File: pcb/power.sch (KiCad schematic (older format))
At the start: 2 parts, among them U100 MCIMX7S5EVM08SC

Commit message: pcb: working on sch
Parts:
- added unit 10 of U100
- gave numbers to parts that had none: 1
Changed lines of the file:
@@
 $EndComp
 $Comp
-L symbols:LTC3456 U?
+L symbols:LTC3456 U1
 U 1 1 5DB1F8DC
 P 8050 3700
-F 0 "U?" H 8050 4765 50  0000 C CNN
+F 0 "U1" H 8050 4765 50  0000 C CNN
 F 1 "LTC3456" H 8050 4674 50  0000 C CNN
 F 2 "" H 8050 3700 50  0001 C CNN
@@
 	1    0    0    -1
 $EndComp
+$Comp
+L symbols:MCIMX7S5EVM08SC U100
+U 10 1 5D65C6CC
+P 5200 7800
+F 0 "U100" H 5200 10165 50  0000 C CNN
+F 1 "MCIMX7S5EVM08SC" H 5200 10074 50  0000 C CNN
+F 2 "footprints:BGA-541_25x25_19.0x19.0mm" H 5200 8500 50  0001 C CNN
+F 3 "" H 5200 8500 50  0001 C CNN
+	10   5200 7800
+	1    0    0    -1
+$EndComp

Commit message: pcb: working on sch
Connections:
- net GND: now reaches U100.AA10 (PCIE_VP)
- net GND: now also U100.AA11 (PCIE_VP_TX), U100.AA12 (PCIE_VP_RX), U100.H12 (USB_VDD_H_1P2), U100.Y10 (PCIE_VPH), U100.Y11 (PCIE_VPH_TX), U100.Y12 (PCIE_VPH_RX)
- no-connect marks 0 -> 4
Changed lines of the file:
@@
 	1    0    0    -1
 $EndComp
+NoConn ~ 3400 2200
+NoConn ~ 3400 2300
+NoConn ~ 3400 3100
+$Comp
+L power:GND #PWR?
+U 1 1 5D1F2E2F
+P 3500 6200
+F 0 "#PWR?" H 3500 5950 50  0001 C CNN
+F 1 "GND" H 3505 6027 50  0000 C CNN
+F 2 "" H 3500 6200 50  0001 C CNN
+F 3 "" H 3500 6200 50  0001 C CNN
+	1    3500 6200
+	1    0    0    -1
+$EndComp
+Wire Wire Line
+	3400 3300 3500 3300
+Wire Wire Line
+	3500 3300 3500 3400
+Wire Wire Line
+	3400 3400 3500 3400
+Connection ~ 3500 3400
+Wire Wire Line
+	3500 3400 3500 3500
+Wire Wire Line
+	3400 3500 3500 3500
+Connection ~ 3500 3500
+Wire Wire Line
+	3500 3500 3500 4700
+NoConn ~ 3400 4500
+Wire Wire Line
+	3400 4700 3500 4700
+Connection ~ 3500 4700
+Wire Wire Line
+	3500 4700 3500 6200
+Wire Wire Line
+	3400 2500 3500 2500
+Wire Wire Line
+	3500 2500 3500 2600
+Connection ~ 3500 3300
+Wire Wire Line
+	3400 2600 3500 2600
+Connection ~ 3500 2600
+Wire Wire Line
+	3500 2600 3500 2700
+Wire Wire Line
+	3400 2700 3500 2700
+Connection ~ 3500 2700
+Wire Wire Line
+	3500 2700 3500 3300
 $EndSCHEMATC

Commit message: pcb: finishing sch for r0.1
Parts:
- removed unit 10 of U100
- added BT: Battery, Battery:BatteryHolder_Keystone_2468_2xAAA, symbol Device:Battery
- added BT_Backup: CR2032, Battery:BatteryHolder_Keystone_1060_1x2032, symbol Device:Battery_Cell
- added C1, C10, C11, C13, C8: 4.7uF, Capacitor_SMD:C_0603_1608Metric, symbol Device:C
- added C12, C4, C9: 220pF, Capacitor_SMD:C_0402_1005Metric, symbol Device:C
- added C14, C2, C3, C7: 10uF, Capacitor_SMD:C_0603_1608Metric, symbol Device:C
- added C15, C16, C17, C18, C20, C21, C22, C23, C25, C26, C27, C28, C29, C30, C32, C33, C34, C35, C36, C37, C38: 220nF, Capacitor_SMD:C_0402_1005Metric, symbol Device:C
- added C19, C24, C5: 22uF, Capacitor_SMD:C_0603_1608Metric, symbol Device:C
- added C31, C39, C40, C41: 2.2uF, Capacitor_SMD:C_0402_1005Metric, symbol Device:C
- added C6: 1uF, Capacitor_SMD:C_0402_1005Metric, symbol Device:C
- added D1, D2: 1N5819, Diode_SMD:D_SOD-123, symbol Device:D_Shockley
- added L1, L3: 10uH, Inductor_SMD:L_Vishay_IHLP-4040, symbol Device:L
- added L2: 4.7uH, Inductor_SMD:L_Vishay_IHLP-4040, symbol Device:L
- added L4, L5: 3.3uH, Inductor_SMD:L_Vishay_IHLP-4040, symbol Device:L
- added L6: 120R, Inductor_SMD:L_0603_1608Metric, symbol Device:L
- added R1: 1K, Resistor_SMD:R_0603_1608Metric, symbol Device:R
- added R10: 130K, Resistor_SMD:R_0603_1608Metric, symbol Device:R
- added R11: 200K, Resistor_SMD:R_0603_1608Metric, symbol Device:R
- added R12, R4, R7: 0R05, Resistor_SMD:R_1210_3225Metric, symbol Device:R
- added R2, R5: 100K, Resistor_SMD:R_0603_1608Metric, symbol Device:R
- added R3, R6: 80.6K, Resistor_SMD:R_0603_1608Metric, symbol Device:R
- added R8: 147K, Resistor_SMD:R_0603_1608Metric, symbol Device:R
- added R9: 154K, Resistor_SMD:R_0603_1608Metric, symbol Device:R
- added U2, U3: LTC3549, Package_DFN_QFN:DFN-6-1EP_3x2mm_P0.5mm_EP1.65x1.35mm, symbol symbols:LTC3549
- U1: footprint (none) -> Package_DFN_QFN:VQFN-24-1EP_4x4mm_P0.5mm_EP2.45x2.45mm_ThermalVias
- U100: footprint (none) -> footprints:BGA-541_25x25_19.0x19.0mm
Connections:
- net GND: now also U1.3 (AGND), U1.6 (PGND), U100.A1 (GND), U100.A13 (GND), U100.A17 (GND), U100.A21 (GND), U100.A25 (GND), U100.A3 (GND), U100.A6 (GND), U100.A9 (GND), U100.AA1 (GND), U100.AA15 (GND), U100.AA2 (GND), U100.AA23 (GND), U100.AA6 (GND), U100.AA8 (GND), U100.AB12 (GND), U100.AB4 (GND), U100.AB5 (GND), U100.AB7 (GND), U100.AB9 (GND), U100.AC12 (GND), U100.AC15 (GND), U100.AC17 (GND), U100.AC19 (GND), U100.AC21 (GND), U100.AC23 (GND), U100.AC6 (GND), U100.AC9 (GND), U100.AD12 (GND), U100.AD2 (GND), U100.AD5 (GND), U100.AD7 (GND), U100.AD9 (GND), U100.AE1 (GND), U100.AE12 (GND), U100.AE24 (GND), U100.AE25 (GND), U100.AE5 (GND), U100.AE7 (GND), U100.AE9 (GND), U100.B13 (GND), U100.B17 (GND), U100.B21 (GND), U100.B3 (GND), U100.B6 (GND), U100.B9 (GND), U100.C13 (GND), U100.C15 (GND), U100.C16 (GND), U100.C18 (GND), U100.C19 (GND), U100.C9 (GND), U100.D1 (GND), U100.D10 (GND), U100.D2 (GND), U100.D22 (GND), U100.D4 (GND), U100.D7 (GND), U100.F11 (GND), U100.F13 (GND), U100.F7 (GND), U100.F8 (GND), U100.G11 (GND), U100.G13 (GND), U100.G15 (GND), U100.G17 (GND), U100.G19 (GND), U100.G22 (GND), U100.G4 (GND), U100.G7 (GND), U100.G9 (GND), U100.H1 (GND), U100.H2 (GND), U100.J19 (GND), U100.J7 (GND), U100.K10 (GND), U100.K12 (GND), U100.K14 (GND), U100.K16 (GND), U100.K22 (GND), U100.K4 (GND), U100.L11 (GND), U100.L13 (GND), U100.L15 (GND), U100.L19 (GND), U100.L7 (GND), U100.M10 (GND), U100.M12 (GND), U100.M14 (GND), U100.M16 (GND), U100.M24 (GND), U100.M25 (GND), U100.N11 (GND), U100.N13 (GND), U100.N15 (GND), U100.N19 (GND), U100.N4 (GND), U100.N7 (GND), U100.P10 (GND), U100.P12 (GND), U100.P14 (GND), U100.P16 (GND), U100.R11 (GND), U100.R13 (GND), U100.R15 (GND), U100.R19 (GND), U100.R20 (GND), U100.R21 (GND), U100.R23 (GND), U100.R7 (GND), U100.T10 (GND), U100.T12 (GND), U100.T14 (GND), U100.T16 (GND), U100.T20 (GND), U100.T4 (GND), U100.U11 (GND), U100.U19 (GND), U100.U20 (GND), U100.U23 (GND), U100.U7 (GND), U100.V20 (GND), U100.W1 (GND), U100.W11 (GND), U100.W13 (GND), U100.W15 (GND), U100.W17 (GND), U100.W19 (GND), U100.W2 (GND), U100.W20 (GND), U100.W23 (GND), U100.W4 (GND), U100.W7 (GND), U100.W9 (GND), U100.Y13 (GND), U100.Y14 (GND), U100.Y15 (GND), U100.Y16 (GND), U100.Y17 (GND), U100.Y18 (GND), U100.Y19 (GND), U100.Y6 (GND), BT.2 (-), BT_Backup.2 (-), C1.2, C10.2, C11.2, C13.2, C14.2, C15.2, C16.2, C17.2, C18.2, C19.2, C2.2, C20.2, C21.2, C22.2, C23.2, C24.2, C25.2, C26.2, C27.2, C28.2, C29.2, C3.2, C30.2, C31.2, C32.2, C33.2, C34.2, C35.2, C36.1, C37.1, C38.1, C39.1, C40.1, C41.1, C5.2, C6.2, C7.2, C8.2, R11.2, R3.1, R6.2, R9.2, U2.2 (GND), U2.4 (MODE), U2.7 (EP), U3.2 (GND), U3.4 (MODE), U3.7 (EP)
- net at U100.AA9 (VDDD_1P0_CAP): now also C36.2
- net at U100.AC5 (VDD_LPSR_1P0_CAP): now also C40.2
- net at U100.AD8 (VDD_SNVS_IN): now also D1.1 (K), D2.1 (K)
- net at U100.AE8 (VDD_SNVS_1P8_CAP): now also C39.2
- net +1V0: now reaches U100.C14 (VDD_SOC_IN)
- net +1V0: now also U100.C17 (VDD_ARM_IN), U100.C20 (VDD_ARM_IN), U100.D14 (VDD_SOC_IN), U100.D17 (VDD_ARM_IN), U100.D20 (VDD_ARM_IN), U100.F18 (VDD_SOC_IN), U100.F19 (VDD_SOC_IN), U100.F22 (VDD_ARM_IN), U100.F23 (VDD_ARM_IN), U100.F3 (VDD_SOC_IN), U100.F4 (VDD_SOC_IN), U100.J22 (VDD_ARM_IN), U100.J23 (VDD_ARM_IN), U100.J3 (VDD_SOC_IN), U100.J4 (VDD_SOC_IN), U100.M3 (VDD_SOC_IN), U100.M4 (VDD_SOC_IN), U100.P18 (VDD_SOC_IN), U100.R17 (VDD_SOC_IN), U100.R3 (VDD_SOC_IN), U100.R4 (VDD_SOC_IN), U100.T18 (VDD_SOC_IN), U100.U13 (VDD_SOC_IN), U100.U15 (VDD_SOC_IN), U100.U17 (VDD_SOC_IN), U100.V12 (VDD_SOC_IN), U100.V14 (VDD_SOC_IN), U100.V16 (VDD_SOC_IN), U100.V18 (VDD_SOC_IN), C14.1, C15.1, C16.1, C17.1, C18.1, C19.1, C20.1, C21.1, C22.1, C23.1, C24.1, C25.1, C26.1, C27.1, C28.1, C29.1, R12.1
- net at U100.H18 (MIPI_VREG_0P4V): now also C38.2
- net +3V3: now reaches U100.P8 (NVCC_GPIO1)
- net +3V3: now also U100.T8 (NVCC_GPIO2), C34.1, C35.1, C7.1, D2.2 (A), R7.1
- net at U100.V10 (PVCC_GPIO_CAP): now also C41.2
- net at U100.V3 (VDDA_1P0_CAP): now also C37.2
- net at U100.V6 (VDDA_1P8): now also U100.W5 (VDDA_1P8), C30.1, C31.1, L6.2
- net +1V8: now reaches U100.V8 (FUSE_FSOURCE)
- net +1V8: now also U100.W6 (VDD_LPSR_IN), C11.1, C2.1, C32.1, C33.1, C8.1, L6.1, R4.2, U2.1 (Vin), U2.5 (RUN), U3.1 (Vin), U3.5 (RUN)
- net at U1.1 (AIN): now also R2.1, R3.2
- net VBUS: now reaches U1.10 (USB)
- net VBUS: now also R1.2
- net at U1.12 (USBHP): now also R1.1
- net at U1.13 (SW2_BK): now also L3.2
- net at U1.14 (SW2_BST): now also L2.2
- net at U1.15 (VINT): now also C5.1, L3.1
- net at U1.16 (VMAIN): now also C6.1, R7.2
- net USB_SUSPEND: now reaches U1.18 (SUSPEND)
- net PWRKEY: now reaches U1.19 (PWRKEY)
- net BAT_LOW: now reaches U1.2 (AO)
- net PB_STAT: now reaches U1.20 (PBSTAT)
- net PMIC_ON_REQ: now reaches U1.21 (PWRON)
- net +BATT: now reaches U1.22 (MODE)
- net +BATT: now also U1.4 (VBAT), BT.1 (+), C1.1, L2.1, R2.2
- net POR: now reaches U1.23 (~RESET)
- net at U1.24 (FB1): now also C4.2, R5.2, R6.1
- net at U1.5 (SW1): now also L1.2
- net EXT_PWR_GOOD: now reaches U1.8 (~EXT_PWR)
- new net: C3.1, C4.1, L1.1, R4.1, R5.1
- new net: L5.1, U3.3 (SW)
- new net: C12.2, R10.2, R11.1, U3.6 (Vfb)
- new net: C12.1, C13.1, L5.2, R10.1, R12.2
- new net: L4.1, U2.3 (SW)
- new net: C9.2, R8.2, R9.1, U2.6 (Vfb)
- new net: BT_Backup.1 (+), D1.2 (A)
- new net +1V2: C10.1, C9.1, L4.2, R8.1
- no-connect marks 4 -> 9
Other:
- note added: "CAP for VDD_ARM"
- note added: "CAP for VDD_SOC"
- note added: "Maximum 150mA\n(Voltage drop 7.5mV)"
- note added: "Maximum 200mA\n(Voltage drop 10mV)"
- note added: "Vfb=0.611V"
- moved on the sheet: U1, U100A

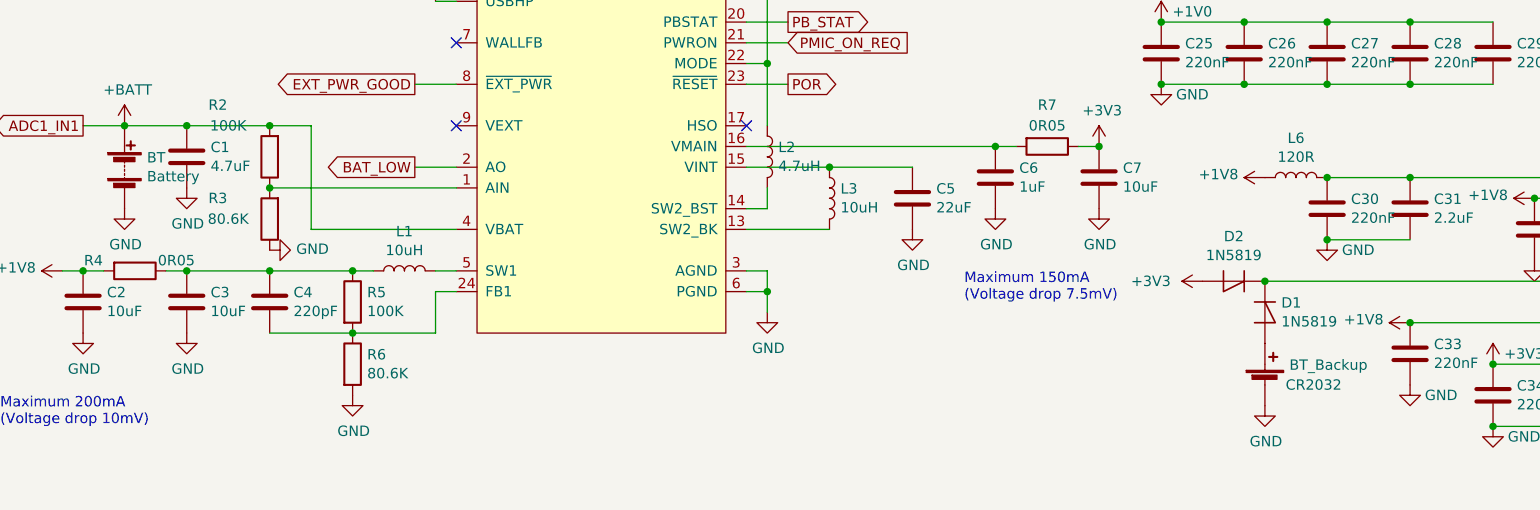
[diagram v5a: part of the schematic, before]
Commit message: pcb: initial netlist
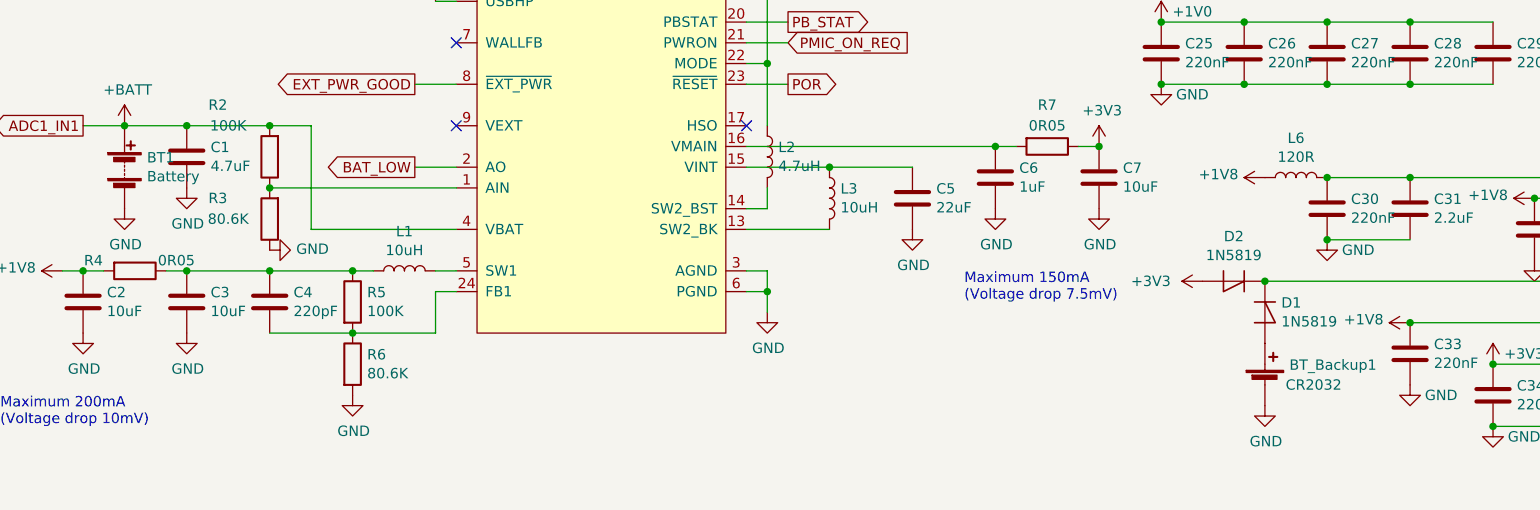
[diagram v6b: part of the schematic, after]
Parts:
- renumbered BT to BT1, BT_Backup to BT_Backup1
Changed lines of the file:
@@
 	3000 4850 3200 4850
 $Comp
-L Device:Battery BT
+L Device:Battery BT1
 U 1 1 5D2E55D4
 P 1600 4850
-F 0 "BT" H 1708 4896 50  0000 L CNN
+F 0 "BT1" H 1708 4896 50  0000 L CNN
 F 1 "Battery" H 1708 4805 50  0000 L CNN
 F 2 "Battery:BatteryHolder_Keystone_2468_2xAAA" V 1600 4910 50  0001 C CNN
@@
 	1400 4650 1600 4650
 $Comp
-L Device:Battery_Cell BT_Backup
+L Device:Battery_Cell BT_Backup1
 U 1 1 5D97B728
 P 7100 5900
-F 0 "BT_Backup" H 7218 5996 50  0000 L CNN
+F 0 "BT_Backup1" H 7218 5996 50  0000 L CNN
 F 1 "CR2032" H 7200 5900 50  0000 L CNN
 F 2 "Battery:BatteryHolder_Keystone_1060_1x2032" V 7100 5960 50  0001 C CNN
@@
 Connection ~ 7100 5400
 $Comp
-L power:GND #PWR?
+L power:GND #PWR0316
 U 1 1 5D98CDD3
 P 7100 6000
-F 0 "#PWR?" H 7100 5750 50  0001 C CNN
+F 0 "#PWR0316" H 7100 5750 50  0001 C CNN
 F 1 "GND" H 7105 5827 50  0000 C CNN
 F 2 "" H 7100 6000 50  0001 C CNN
@@
 $EndComp
 $Comp
-L power:+3V3 #PWR?
+L power:+3V3 #PWR0317
 U 1 1 5D98CE2E
 P 6800 5400
-F 0 "#PWR?" H 6800 5250 50  0001 C CNN
+F 0 "#PWR0317" H 6800 5250 50  0001 C CNN
 F 1 "+3V3" V 6800 5650 50  0000 C CNN
 F 2 "" H 6800 5400 50  0001 C CNN

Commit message: pcb: working on layout
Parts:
- added D3: LED, LED_THT:LED_D5.0mm, symbol Device:LED
- added R13: 1K, Resistor_SMD:R_0603_1608Metric, symbol Device:R
- added SW1: SW_SPDT, Button_Switch_SMD:SW_SPDT_PCM12, symbol Switch:SW_SPDT
- BT_Backup1: footprint Battery:BatteryHolder_Keystone_1060_1x2032 -> footprints:BatteryHolder_CR1220
- L1, L2, L3, L4, L5: footprint Inductor_SMD:L_Vishay_IHLP-4040 -> Inductor_SMD:L_Vishay_IHLP-1212
- L6: footprint Inductor_SMD:L_0603_1608Metric -> Inductor_SMD:L_0402_1005Metric
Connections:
- net EXT_PWR_GOOD: now also D3.2 (A)
- net GND: now also R13.2, SW1.3 (C)
- net PWRKEY renamed PWR_KEY
- net PWR_KEY: now also SW1.2 (B)
- new net: D3.1 (K), R13.1
- no-connect marks 9 -> 10
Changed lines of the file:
@@
 EXT_PWR_GOOD
 Wire Wire Line
-	3000 4450 3200 4450
+	3000 4450 3100 4450
 NoConn ~ 3200 4250
 NoConn ~ 3200 4650
@@
 F 0 "L1" V 3140 5350 50  0000 C CNN
 F 1 "10uH" V 3049 5350 50  0000 C CNN
-F 2 "Inductor_SMD:L_Vishay_IHLP-4040" H 2950 5350 50  0001 C CNN
+F 2 "Inductor_SMD:L_Vishay_IHLP-1212" H 2950 5350 50  0001 C CNN
 F 3 "~" H 2950 5350 50  0001 C CNN
 	1    2950 5350
@@
 	1500 5350 1400 5350
 NoConn ~ 4600 3750
-Text GLabel 4800 3950 2    50   Input ~ 0
-PWRKEY
 Text GLabel 4800 4150 2    50   Output ~ 0
 PB_STAT
@@
 Wire Wire Line
 	4600 4150 4800 4150
-Wire Wire Line
-	4600 3950 4800 3950
 NoConn ~ 4600 4650
 $Comp
@@
 F 0 "L3" H 5053 5046 50  0000 L CNN
 F 1 "10uH" H 5053 4955 50  0000 L CNN
-F 2 "Inductor_SMD:L_Vishay_IHLP-4040" H 5000 5000 50  0001 C CNN
+F 2 "Inductor_SMD:L_Vishay_IHLP-1212" H 5000 5000 50  0001 C CNN
 F 3 "~" H 5000 5000 50  0001 C CNN
 	1    5000 5000
@@
 F 0 "L2" H 4753 4846 50  0000 L CNN
 F 1 "4.7uH" H 4753 4755 50  0000 L CNN
-F 2 "Inductor_SMD:L_Vishay_IHLP-4040" H 4700 4800 50  0001 C CNN
+F 2 "Inductor_SMD:L_Vishay_IHLP-1212" H 4700 4800 50  0001 C CNN
 F 3 "~" H 4700 4800 50  0001 C CNN
 	1    4700 4800
@@
 F 0 "L5" V 7240 1700 50  0000 C CNN
 F 1 "3.3uH" V 7149 1700 50  0000 C CNN
-F 2 "Inductor_SMD:L_Vishay_IHLP-4040" H 7050 1700 50  0001 C CNN
+F 2 "Inductor_SMD:L_Vishay_IHLP-1212" H 7050 1700 50  0001 C CNN
 F 3 "~" H 7050 1700 50  0001 C CNN
 	1    7050 1700
@@
 F 0 "L4" V 3640 1700 50  0000 C CNN
 F 1 "3.3uH" V 3549 1700 50  0000 C CNN
-F 2 "Inductor_SMD:L_Vishay_IHLP-4040" H 3450 1700 50  0001 C CNN
+F 2 "Inductor_SMD:L_Vishay_IHLP-1212" H 3450 1700 50  0001 C CNN
 F 3 "~" H 3450 1700 50  0001 C CNN
 	1    3450 1700
@@
 F 0 "L6" V 7440 4900 50  0000 C CNN
 F 1 "120R" V 7349 4900 50  0000 C CNN
-F 2 "Inductor_SMD:L_0603_1608Metric" H 7250 4900 50  0001 C CNN
+F 2 "Inductor_SMD:L_0402_1005Metric" H 7250 4900 50  0001 C CNN
 F 3 "~" H 7250 4900 50  0001 C CNN
 	1    7250 4900
@@
 F 0 "BT_Backup1" H 7218 5996 50  0000 L CNN
 F 1 "CR2032" H 7200 5900 50  0000 L CNN
-F 2 "Battery:BatteryHolder_Keystone_1060_1x2032" V 7100 5960 50  0001 C CNN
+F 2 "footprints:BatteryHolder_CR1220" V 7100 5960 50  0001 C CNN
 F 3 "~" V 7100 5960 50  0001 C CNN
 	1    7100 5900
@@
 	0    -1   -1   0
 $EndComp
+$Comp
+L Switch:SW_SPDT SW1
+U 1 1 5D82E996
+P 5500 3950
+F 0 "SW1" H 5500 4235 50  0000 C CNN
+F 1 "SW_SPDT" H 5500 4144 50  0000 C CNN
+F 2 "Button_Switch_SMD:SW_SPDT_PCM12" H 5500 3950 50  0001 C CNN
+F 3 "~" H 5500 3950 50  0001 C CNN
+	1    5500 3950
+	1    0    0    -1
+$EndComp
+$Comp
+L power:GND #PWR0318
+U 1 1 5D830E91
+P 5800 4150
+F 0 "#PWR0318" H 5800 3900 50  0001 C CNN
+F 1 "GND" H 5805 3977 50  0000 C CNN
+F 2 "" H 5800 4150 50  0001 C CNN
+F 3 "" H 5800 4150 50  0001 C CNN
+	1    5800 4150
+	1    0    0    -1
+$EndComp
+Text Label 4800 3950 0    50   ~ 0
+PWR_KEY
+Wire Wire Line
+	4600 3950 5300 3950
+Wire Wire Line
+	5700 4050 5800 4050
+Wire Wire Line
+	5800 4050 5800 4150
+NoConn ~ 5700 3850
+$Comp
+L Device:LED D3
+U 1 1 5D86EEEC
+P 2850 4250
+F 0 "D3" H 2800 4350 50  0000 C CNN
+F 1 "LED" H 2950 4350 50  0000 C CNN
+F 2 "LED_THT:LED_D5.0mm" H 2850 4250 50  0001 C CNN
+F 3 "~" H 2850 4250 50  0001 C CNN
+	1    2850 4250
+	1    0    0    -1
+$EndComp
+$Comp
+L Device:R R13
+U 1 1 5D86FBD0
+P 2550 4250
+F 0 "R13" V 2450 4150 50  0000 C CNN
+F 1 "1K" V 2450 4300 50  0000 C CNN
+F 2 "Resistor_SMD:R_0603_1608Metric" V 2480 4250 50  0001 C CNN
+F 3 "~" H 2550 4250 50  0001 C CNN
+	1    2550 4250
+	0    1    1    0
+$EndComp
+$Comp
+L power:GND #PWR0319
+U 1 1 5D870814
+P 2300 4350
+F 0 "#PWR0319" H 2300 4100 50  0001 C CNN
+F 1 "GND" H 2305 4177 50  0000 C CNN
+F 2 "" H 2300 4350 50  0001 C CNN
+F 3 "" H 2300 4350 50  0001 C CNN
+	1    2300 4350
+	1    0    0    -1
+$EndComp
+Wire Wire Line
+	2400 4250 2300 4250
+Wire Wire Line
+	2300 4250 2300 4350
+Wire Wire Line
+	3000 4250 3100 4250
+Wire Wire Line
+	3100 4250 3100 4450
+Connection ~ 3100 4450
+Wire Wire Line
+	3100 4450 3200 4450
 $EndSCHEMATC

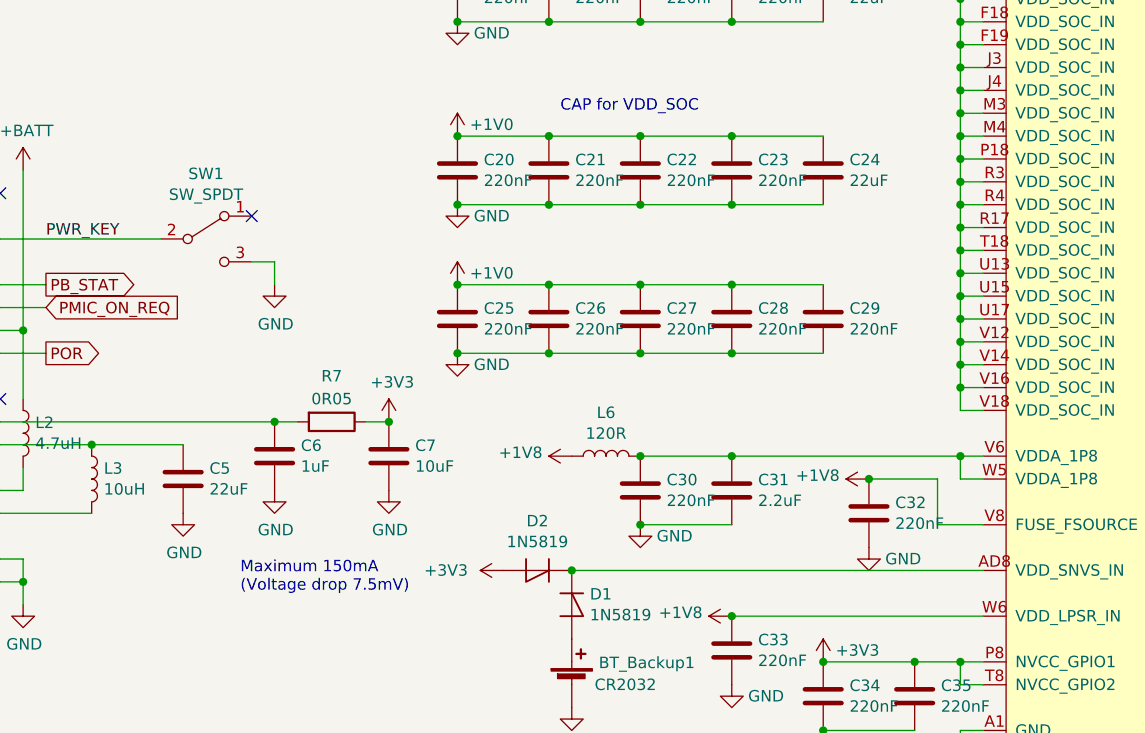
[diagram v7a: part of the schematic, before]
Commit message: pcb: add board outline
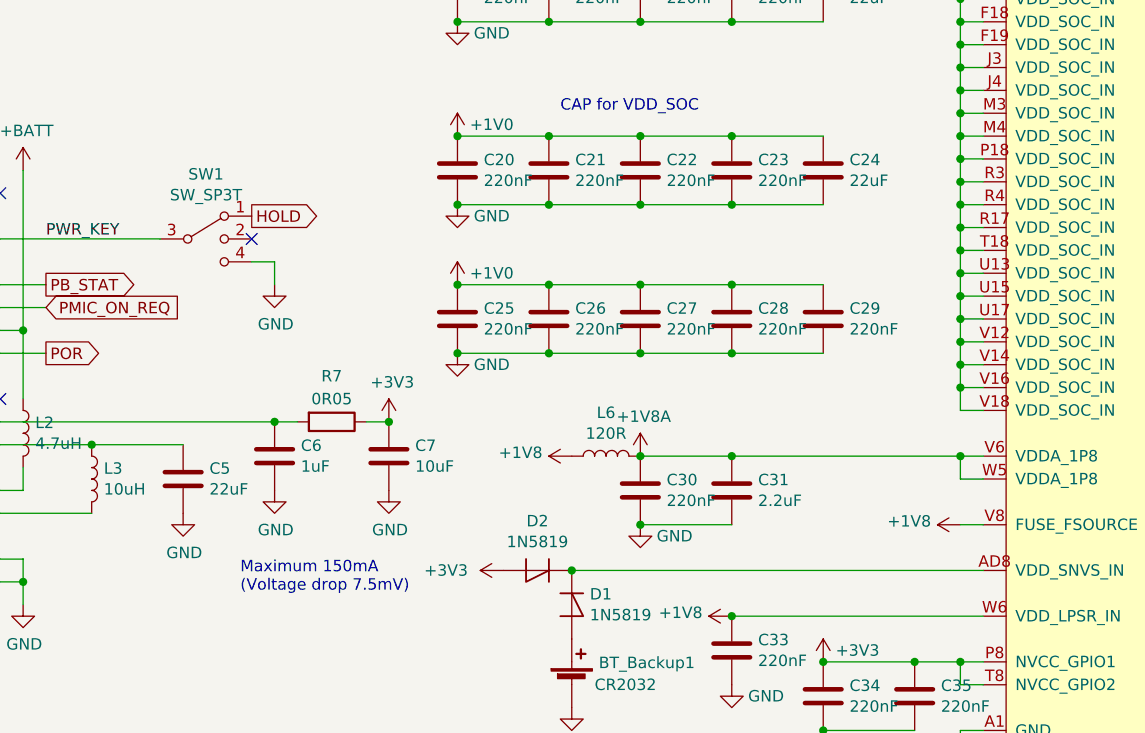
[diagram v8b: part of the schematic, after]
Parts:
- removed C32: 220nF, Capacitor_SMD:C_0402_1005Metric, symbol Device:C
- removed SW1: SW_SPDT, Button_Switch_SMD:SW_SPDT_PCM12, symbol Switch:SW_SPDT
- added SW1: SW_SP3T, footprints:SW_SP3T_JSM0701SAQNL, symbol Switch:SW_SP3T
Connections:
- net GND: now also SW1.4
- net PWR_KEY: now also SW1.3
- net +1V8A: now reaches C30.1, C31.1, L6.2, U100.V6 (VDDA_1P8), U100.W5 (VDDA_1P8)
- new net HOLD: SW1.1
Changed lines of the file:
@@
 L power:+1V8 #PWR0164
 U 1 1 5D6419DC
-P 8400 5000
-F 0 "#PWR0164" H 8400 4850 50  0001 C CNN
-F 1 "+1V8" V 8415 5128 50  0000 L CNN
-F 2 "" H 8400 5000 50  0001 C CNN
-F 3 "" H 8400 5000 50  0001 C CNN
-	1    8400 5000
+P 8800 5200
+F 0 "#PWR0164" H 8800 5050 50  0001 C CNN
+F 1 "+1V8" V 8815 5328 50  0000 L CNN
+F 2 "" H 8800 5200 50  0001 C CNN
+F 3 "" H 8800 5200 50  0001 C CNN
+	1    8800 5200
 	0    -1   -1   0
 $EndComp
-$Comp
-L Device:C C?
-U 1 1 5D642009
-P 8400 5150
-AR Path="/5D5090CA/5D642009" Ref="C?"  Part="1"
-AR Path="/5D4C99F9/5D642009" Ref="C32"  Part="1"
-F 0 "C32" H 8515 5196 50  0000 L CNN
-F 1 "220nF" H 8515 5105 50  0000 L CNN
-F 2 "Capacitor_SMD:C_0402_1005Metric" H 8438 5000 50  0001 C CNN
-F 3 "~" H 8400 5150 50  0001 C CNN
-	1    8400 5150
-	1    0    0    -1
-$EndComp
-$Comp
-L power:GND #PWR?
-U 1 1 5D642499
-P 8400 5300
-AR Path="/5D5090CA/5D642499" Ref="#PWR?"  Part="1"
-AR Path="/5D4C99F9/5D642499" Ref="#PWR0165"  Part="1"
-F 0 "#PWR0165" H 8400 5050 50  0001 C CNN
-F 1 "GND" H 8550 5250 50  0000 C CNN
-F 2 "" H 8400 5300 50  0001 C CNN
-F 3 "" H 8400 5300 50  0001 C CNN
-	1    8400 5300
-	1    0    0    -1
-$EndComp
-Wire Wire Line
-	8900 5200 8700 5200
-Wire Wire Line
-	8700 5200 8700 5000
-Wire Wire Line
-	8700 5000 8400 5000
-Connection ~ 8400 5000
+Wire Wire Line
+	8900 5200 8800 5200
 Wire Wire Line
 	8900 5400 7100 5400
@@
 $EndComp
 $Comp
-L Switch:SW_SPDT SW1
-U 1 1 5D82E996
-P 5500 3950
-F 0 "SW1" H 5500 4235 50  0000 C CNN
-F 1 "SW_SPDT" H 5500 4144 50  0000 C CNN
-F 2 "Button_Switch_SMD:SW_SPDT_PCM12" H 5500 3950 50  0001 C CNN
-F 3 "~" H 5500 3950 50  0001 C CNN
-	1    5500 3950
-	1    0    0    -1
-$EndComp
-$Comp
 L power:GND #PWR0318
 U 1 1 5D830E91
@@
 Wire Wire Line
 	5800 4050 5800 4150
-NoConn ~ 5700 3850
+NoConn ~ 5700 3950
 $Comp
 L Device:LED D3
@@
 Wire Wire Line
 	3100 4450 3200 4450
+$Comp
+L symbols:+1V8A #PWR0121
+U 1 1 5D24658B
+P 7400 4900
+F 0 "#PWR0121" H 7400 4750 50  0001 C CNN
+F 1 "+1V8A" H 7415 5073 50  0000 C CNN
+F 2 "" H 7400 4900 50  0001 C CNN
+F 3 "" H 7400 4900 50  0001 C CNN
+	1    7400 4900
+	1    0    0    -1
+$EndComp
+$Comp
+L Switch:SW_SP3T SW1
+U 1 1 5D24F9B8
+P 5500 3950
+F 0 "SW1" H 5500 4233 50  0000 C CNN
+F 1 "SW_SP3T" H 5500 4142 50  0000 C CNN
+F 2 "footprints:SW_SP3T_JSM0701SAQNL" H 4875 4125 50  0001 C CNN
+F 3 "~" H 4875 4125 50  0001 C CNN
+	1    5500 3950
+	1    0    0    -1
+$EndComp
+Text GLabel 5700 3850 2    50   Output ~ 0
+HOLD
 $EndSCHEMATC
